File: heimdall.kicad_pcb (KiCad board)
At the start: 2 copper layers, 50 x 50 mm, 12 parts, among them P1 CONN, U1 ESP-01, U2 TLP222A, U3 UA78M33CDCY

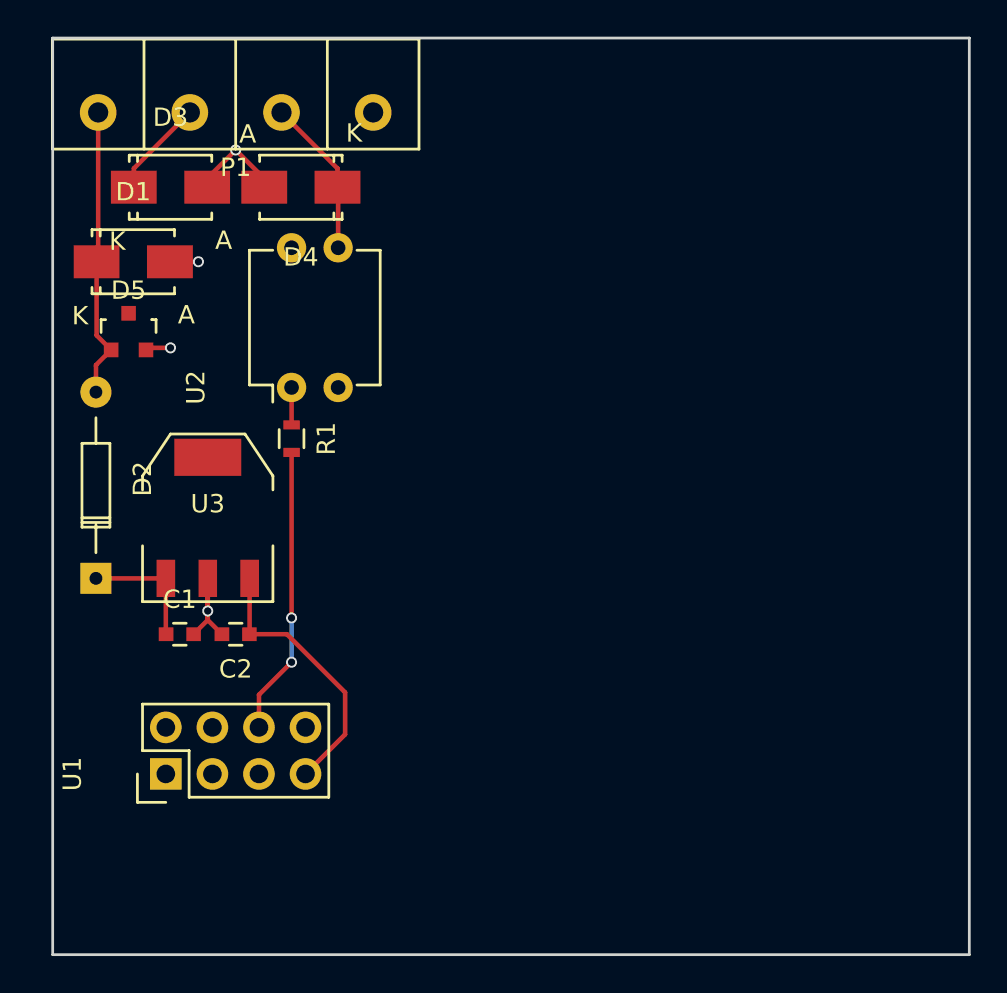
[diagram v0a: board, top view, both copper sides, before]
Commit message: Updated some componants and shuffled PCB
Signed-off-by: Thomas Bytheway <tb403@cam.ac.uk>
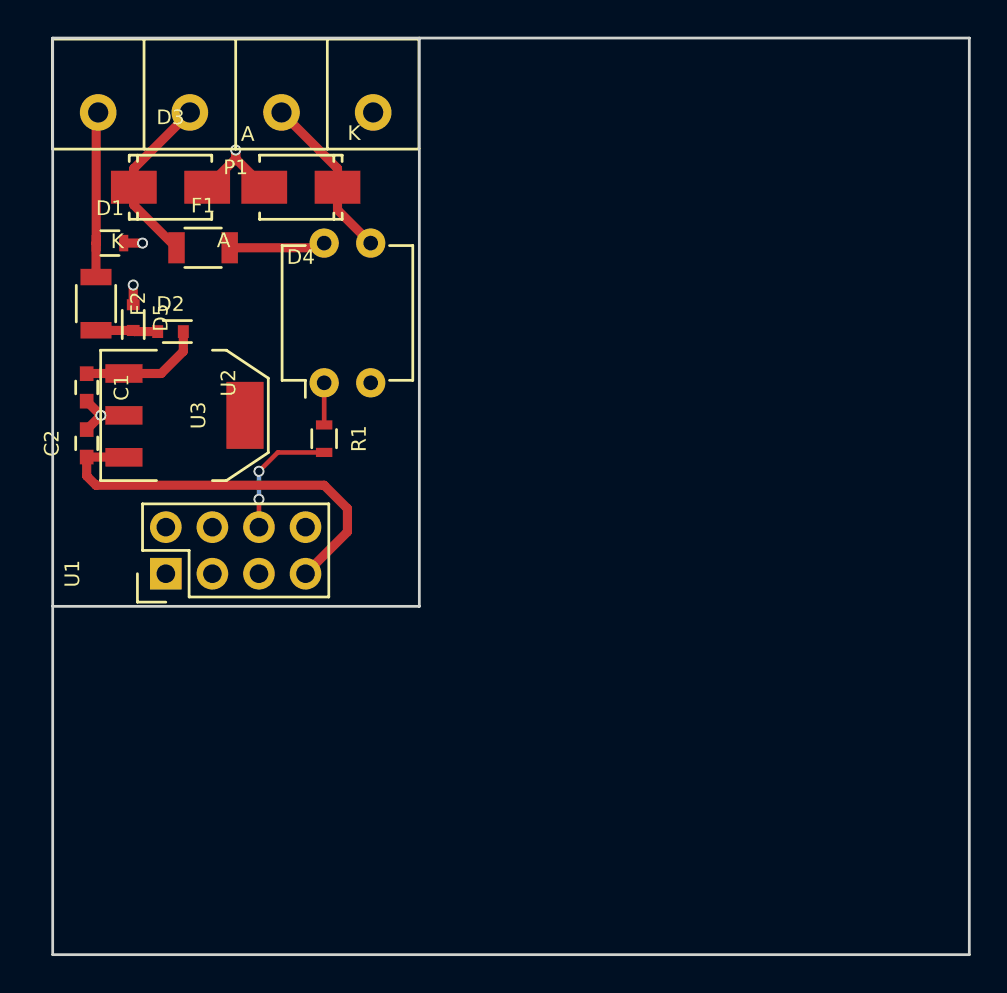
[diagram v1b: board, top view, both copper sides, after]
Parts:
- added F1: 0.5A, Resistors_SMD:R_1206, F.Cu at (108.2, 91.4)
- added F2: 0.25A, Resistors_SMD:R_1206, F.Cu at (102.4, 94.5)
- D1: footprint Diodes_SMD:SMA_Standard -> Resistors_SMD:R_0603
- D2: footprint Diodes_ThroughHole:Diode_DO-35_SOD27_Horizontal_RM10 -> Diodes_SMD:SOD-523
- D5: value 30v -> 22v; footprint TO_SOT_Packages_SMD:SOT-23 -> Diodes_SMD:SOD-523
- moved C1 14.4 mm to (101.9, 99.1), turned to 270 degrees
- moved D2 14.1 mm to (106.4, 96.0), turned to 0 degrees
- moved C2 13.2 mm to (101.9, 102.1), turned to 90 degrees
- moved U1 10.9 mm to (106.2, 109.2)
- moved U3 5.73 mm to (107.2, 100.6), turned to 270 degrees
- moved U2 1.80 mm to (114.8, 98.8)
- moved R1 1.78 mm to (114.8, 101.9)
- moved D1 1.63 mm to (103.1, 91.2)
- moved D5 0.80 mm to (104.4, 95.2), turned to 270 degrees
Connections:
- D2 pad 2: /VCC_IN -> Net-(D2-Pad2)
- D5 pad 1: /VCC_IN -> Net-(D2-Pad2)
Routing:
- net /RELAY_TRIGGER: track 15.7 -> 7.03 mm
- net +3V3: track 14.9 -> 22.5 mm
- net /VCC_IN: track 16.0 -> 9.20 mm
- net /SW0: track 0.00 -> 5.26 mm
- net /SW0_IN: track 5.35 -> 9.61 mm
- net Net-(D2-Pad2): track 0.00 -> 3.48 mm
- net GND: track 15.5 -> 12.1 mm
- net /SW1: track 8.95 -> 9.48 mm
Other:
- outline, holes or cut-outs redrawn
- rule trace_min: 0.2 -> 0.1

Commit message: Slight schematic faffing, more PCB juggling and sexification.
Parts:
- removed D2: D_Small, Diodes_SMD:SOD-523
- removed D5: 22v, Diodes_SMD:SOD-523
- added C3: 104, Capacitors_SMD:C_0603, F.Cu at (102.5, 109.3)
- added C4: 104, Capacitors_SMD:C_0603, F.Cu at (117.0, 109.2)
- added C5: 226, Capacitors_SMD:C_1206, F.Cu at (117.1, 103.8)
- C1: value 0.33uF -> 334
- C2: value 0.1uF -> 104
- U1: footprint Pin_Headers:Pin_Header_Straight_2x04 -> Socket_Strips:Socket_Strip_Straight_2x04
- moved C2 7.24 mm to (109.1, 101.9), turned to 180 degrees
- moved F2 5.95 mm to (101.6, 100.4)
- moved C1 5.14 mm to (106.2, 101.9), turned to 0 degrees
- moved F1 5.02 mm to (104.3, 88.3), turned to 270 degrees
- moved U3 4.21 mm to (107.6, 96.4), turned to 0 degrees
- moved U1 2.60 mm to (106.2, 106.6), turned to 0 degrees
- moved D3 2.54 mm to (109.0, 88.1)
- moved D4 2.41 mm to (116.0, 88.1)
- moved R1 1.37 mm to (114.0, 100.7), turned to 180 degrees
- moved D1 1.05 mm to (102.2, 91.6)
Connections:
- F2 pad 2: Net-(D2-Pad2) -> Net-(C1-Pad1)
- U1 pad 1: Net-(U1-Pad1) -> GND
- U1 pad 2: GND -> Net-(U1-Pad2)
- U1 pad 5: Net-(U1-Pad5) -> /RELAY_TRIGGER
- U1 pad 6: /RELAY_TRIGGER -> Net-(C3-Pad1)
- U1 pad 7: +3V3 -> Net-(U1-Pad7)
- U1 pad 8: Net-(U1-Pad8) -> +3V3
- U3 pad 4: (no net) -> GND
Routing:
- net GND: track 12.1 -> 22.2 mm, vias 4 -> 10
- net Net-(C3-Pad1): track 0.00 -> 9.90 mm
- net /VCC_IN: track 9.20 -> 15.8 mm
- net /SW0: track 5.26 -> 11.1 mm
- net +3V3: track 22.5 -> 17.0 mm
- net Net-(D2-Pad2): track 3.48 -> 0.00 mm
- net /SW0_IN: track 9.61 -> 7.52 mm
- net /SW1: track 9.48 -> 10.5 mm
- net Net-(C1-Pad1): track 6.86 -> 6.02 mm
- added copper zone on F.Cu, net GND
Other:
- board size 50 x 50 mm -> 20 x 32 mm
- board text added: "+"
- board text added: "-"
- board text added: "GND"
- board text added: "Hark <pcb@harkonen.net> Heimdall V1 18/05/16 https://goo.gl/4EXW3O"
- board text added: "SW0"
- board text added: "SW1"
- board text added: "VCC"

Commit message: Much faffing, many switch mode supply, very PCB.
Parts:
- added C6: 2u2, Capacitors_SMD:C_0603, F.Cu at (107.1, 94.1)
- added L1: 10u, Wurth:WE-TPC, F.Cu at (107.8, 99.5)
- added Q1: FDN304P, Housings_SSOT:SuperSOT-3, F.Cu at (119.2, 100.3)
- added R2: 100K, Resistors_SMD:R_0603, F.Cu at (110.5, 102.7)
- added R3: 1K, Resistors_SMD:R_0603, F.Cu at (114.6, 103.1)
- C1: value 334 -> 22u
- C2, C3, C4: value 104 -> 100n
- C5: value 226 -> 22u; footprint Capacitors_SMD:C_1206 -> Capacitors_SMD:C_0603
- F2: value 0.25A -> 0.5A
- R1: footprint Resistors_SMD:R_0603 -> Resistors_SMD:R_1206
- U1: footprint Socket_Strips:Socket_Strip_Straight_2x04 -> esp:ESP-01-NoSilk
- U3: value UA78M33CDCY -> TPS62177; footprint TO_SOT_Packages_SMD:SOT-223 -> Housing_WSON:WSON-10
- moved F2 16.8 mm to (117.6, 105.7), turned to 180 degrees
- moved P1 7.55 mm to (102.5, 84.0)
- moved C2 7.12 mm to (116.1, 103.1), turned to 90 degrees
- moved C1 5.85 mm to (108.2, 96.4), turned to 90 degrees
- moved C5 4.70 mm to (117.9, 108.4), turned to 90 degrees
- moved U1 4.02 mm to (110.0, 107.9)
- moved D1 3.14 mm to (101.7, 88.5)
- moved R1 2.49 mm to (112.5, 102.7), turned to 270 degrees
- moved C3 1.51 mm to (103.8, 108.5)
- moved U3 1.22 mm to (106.8, 95.5), turned to 270 degrees
- moved C4 1.06 mm to (116.4, 108.4), turned to 90 degrees
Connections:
- C1 pad 1: Net-(C1-Pad1) -> +3V3
- C2 pad 1: +3V3 -> /PWROUT
- C2 pad 2: GND -> Net-(C2-Pad2)
- C4 pad 1: +3V3 -> Net-(C4-Pad1)
- C5 pad 1: +3V3 -> Net-(C4-Pad1)
- D1 pad 1: /VCC_IN -> /VCC
- F2 pad 1: /VCC_IN -> Net-(C4-Pad1)
- F2 pad 2: Net-(C1-Pad1) -> /PWROUT
- P1 pad 1: /VCC_IN -> /VCC
- U1 pad 2: Net-(U1-Pad2) -> (no net)
- U1 pad 3: Net-(U1-Pad3) -> (no net)
- U1 pad 4: Net-(U1-Pad4) -> Net-(C4-Pad1)
- U1 pad 7: Net-(U1-Pad7) -> (no net)
- U1 pad 8: +3V3 -> Net-(C4-Pad1)
- U3 pad 1: Net-(C1-Pad1) -> GND
- U3 pad 2: GND -> /VCC
- U3 pad 3: +3V3 -> /VCC
- U3 pad 4: GND -> (no net)
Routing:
- net /PG: track 0.00 -> 16.8 mm
- net /VCC: track 0.00 -> 16.5 mm
- net +3V3: track 17.0 -> 33.4 mm
- net /VCC_IN: track 15.8 -> 0.00 mm
- net Net-(C4-Pad1): track 0.00 -> 14.0 mm
- net Net-(L1-Pad1): track 0.00 -> 6.93 mm
- net Net-(C1-Pad1): track 6.02 -> 0.00 mm
- net Net-(C2-Pad2): track 0.00 -> 5.44 mm
- net GND: track 22.2 -> 26.8 mm, vias 10 -> 4
- net /PWROUT: track 0.00 -> 4.48 mm
- net /RELAY_TRIGGER: track 6.82 -> 3.51 mm, vias 2 -> 0
- net Net-(R1-Pad1): track 1.91 -> 3.39 mm
- net Net-(C3-Pad1): track 9.90 -> 8.59 mm
- removed copper zone on F.Cu, net GND
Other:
- board text added: "Hark <pcb@harkonen.net> Heimdall V1 08/06/16 http://github.com/HarkonenBade/heimdall"
- board text removed: "Hark <pcb@harkonen.net> Heimdall V1 18/05/16 https://goo.gl/4EXW3O"
